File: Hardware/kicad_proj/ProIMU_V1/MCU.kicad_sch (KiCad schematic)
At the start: 8 parts

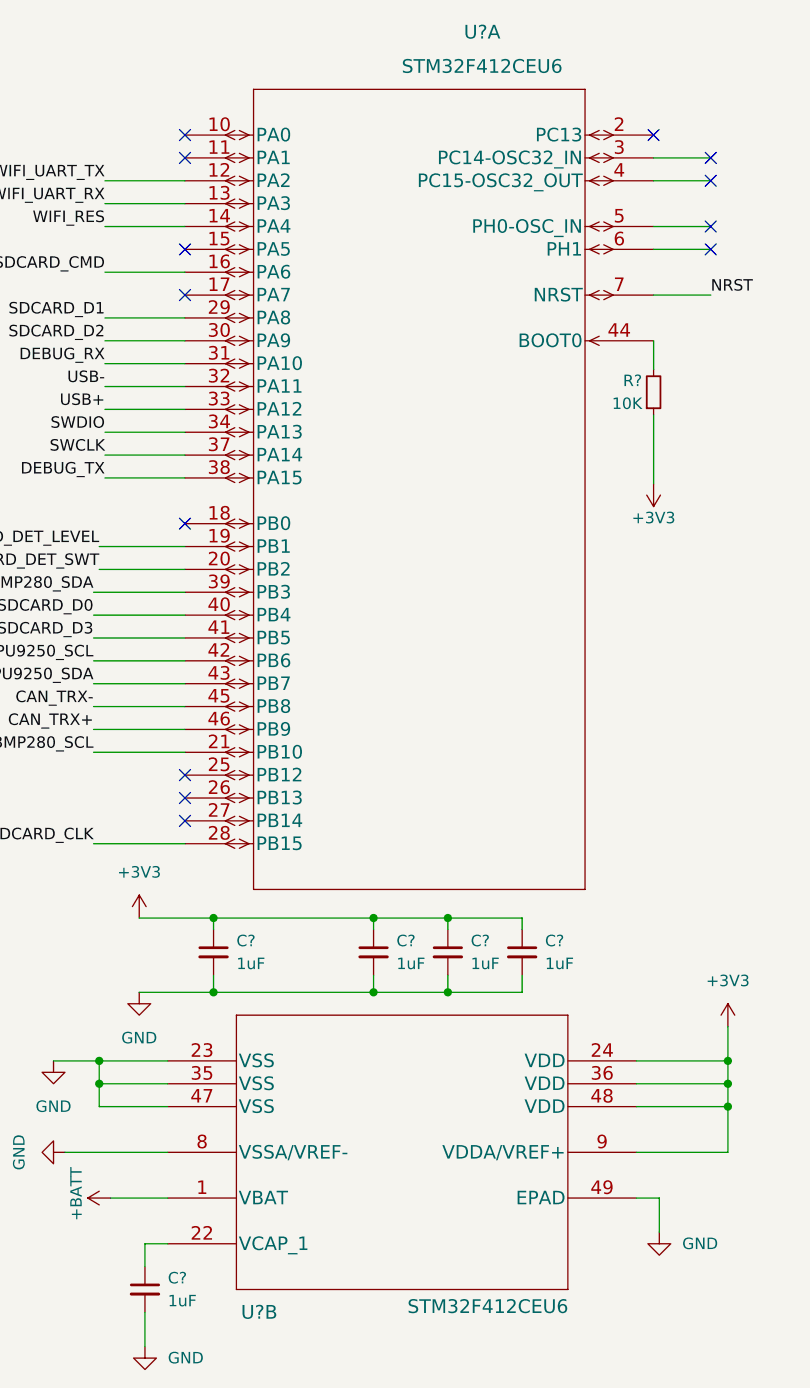
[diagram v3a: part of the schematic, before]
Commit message: Layout Updated. CAN and RS485 section to be updated
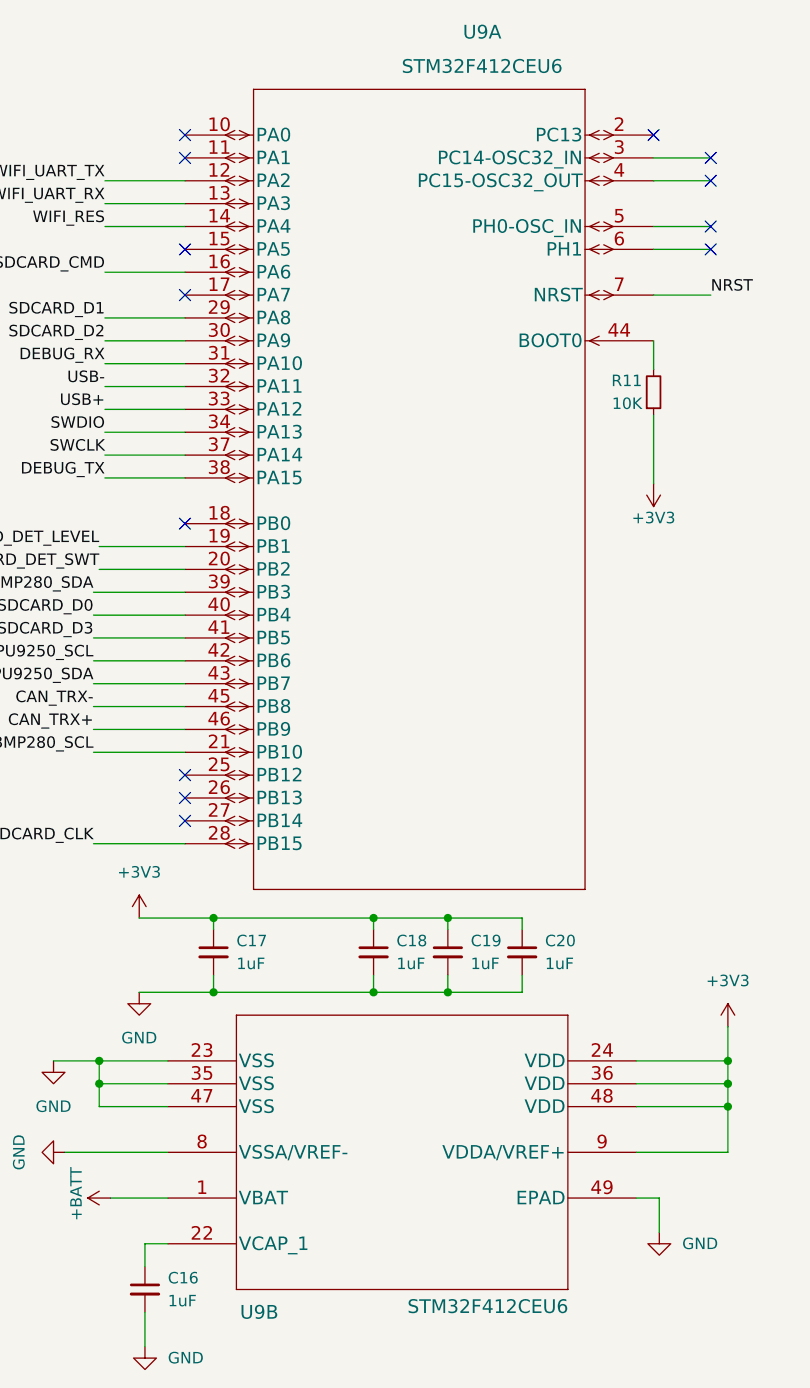
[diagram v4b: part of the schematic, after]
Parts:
- gave numbers to parts that had none: 7
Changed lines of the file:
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@@
   (symbol (lib_id "power:+3V3") (at 163.195 73.025 180) (unit 1)
     (in_bom yes) (on_board yes)
-    (property "Reference" "#PWR?" (id 0) (at 163.195 69.215 0)
+    (property "Reference" "#PWR061" (id 0) (at 163.195 69.215 0)
       (effects (font (size 1.27 1.27)) hide)
     )
@@
   (symbol (lib_id "2022-02-05_19-28-45:STM32F412CEU6") (at 109.22 137.16 0) (unit 2)
     (in_bom yes) (on_board yes)
-    (property "Reference" "U?" (id 0) (at 119.38 165.1 0)
+    (property "Reference" "U9" (id 0) (at 119.38 165.1 0)
       (effects (font (size 1.524 1.524)))
     )
@@
   (symbol (lib_id "Device:C_Small") (at 148.59 125.095 0) (unit 1)
     (in_bom yes) (on_board yes) (fields_autoplaced)
-    (property "Reference" "C?" (id 0) (at 151.13 123.8312 0)
+    (property "Reference" "C20" (id 0) (at 151.13 123.8312 0)
       (effects (font (size 1.27 1.27)) (justify left))
     )
@@
   (symbol (lib_id "power:+3V3") (at 106.045 121.285 0) (unit 1)
     (in_bom yes) (on_board yes) (fields_autoplaced)
-    (property "Reference" "#PWR?" (id 0) (at 106.045 125.095 0)
+    (property "Reference" "#PWR058" (id 0) (at 106.045 125.095 0)
       (effects (font (size 1.27 1.27)) hide)
     )
@@
   (symbol (lib_id "power:+BATT") (at 102.87 152.4 90) (unit 1)
     (in_bom yes) (on_board yes)
-    (property "Reference" "#PWR?" (id 0) (at 106.68 152.4 0)
+    (property "Reference" "#PWR057" (id 0) (at 106.68 152.4 0)
       (effects (font (size 1.27 1.27)) hide)
     )
@@
   (symbol (lib_id "power:GND") (at 163.83 156.21 0) (unit 1)
     (in_bom yes) (on_board yes) (fields_autoplaced)
-    (property "Reference" "#PWR?" (id 0) (at 163.83 162.56 0)
+    (property "Reference" "#PWR062" (id 0) (at 163.83 162.56 0)
       (effects (font (size 1.27 1.27)) hide)
     )
@@
   (symbol (lib_id "power:GND") (at 106.045 129.54 0) (unit 1)
     (in_bom yes) (on_board yes) (fields_autoplaced)
-    (property "Reference" "#PWR?" (id 0) (at 106.045 135.89 0)
+    (property "Reference" "#PWR059" (id 0) (at 106.045 135.89 0)
       (effects (font (size 1.27 1.27)) hide)
     )
@@
   (symbol (lib_id "power:+3V3") (at 171.45 133.35 0) (unit 1)
     (in_bom yes) (on_board yes) (fields_autoplaced)
-    (property "Reference" "#PWR?" (id 0) (at 171.45 137.16 0)
+    (property "Reference" "#PWR063" (id 0) (at 171.45 137.16 0)
       (effects (font (size 1.27 1.27)) hide)
     )
@@
   (symbol (lib_id "Device:R_Small") (at 163.195 62.865 0) (mirror x) (unit 1)
     (in_bom yes) (on_board yes)
-    (property "Reference" "R?" (id 0) (at 161.925 61.595 0)
+    (property "Reference" "R11" (id 0) (at 161.925 61.595 0)
       (effects (font (size 1.27 1.27)) (justify right))
     )
@@
   (symbol (lib_id "power:GND") (at 97.79 147.32 270) (unit 1)
     (in_bom yes) (on_board yes) (fields_autoplaced)
-    (property "Reference" "#PWR?" (id 0) (at 91.44 147.32 0)
+    (property "Reference" "#PWR056" (id 0) (at 91.44 147.32 0)
       (effects (font (size 1.27 1.27)) hide)
     )
@@
   (symbol (lib_id "power:GND") (at 96.52 137.16 0) (unit 1)
     (in_bom yes) (on_board yes) (fields_autoplaced)
-    (property "Reference" "#PWR?" (id 0) (at 96.52 143.51 0)
+    (property "Reference" "#PWR055" (id 0) (at 96.52 143.51 0)
       (effects (font (size 1.27 1.27)) hide)
     )
@@
   (symbol (lib_id "power:GND") (at 106.68 168.91 0) (unit 1)
     (in_bom yes) (on_board yes)
-    (property "Reference" "#PWR?" (id 0) (at 106.68 175.26 0)
+    (property "Reference" "#PWR060" (id 0) (at 106.68 175.26 0)
       (effects (font (size 1.27 1.27)) hide)
     )
@@
   (symbol (lib_id "Device:C_Small") (at 106.68 162.56 0) (unit 1)
     (in_bom yes) (on_board yes) (fields_autoplaced)
-    (property "Reference" "C?" (id 0) (at 109.22 161.2962 0)
+    (property "Reference" "C16" (id 0) (at 109.22 161.2962 0)
       (effects (font (size 1.27 1.27)) (justify left))
     )
@@
   (symbol (lib_id "Device:C_Small") (at 140.335 125.095 0) (unit 1)
     (in_bom yes) (on_board yes) (fields_autoplaced)
-    (property "Reference" "C?" (id 0) (at 142.875 123.8312 0)
+    (property "Reference" "C19" (id 0) (at 142.875 123.8312 0)
       (effects (font (size 1.27 1.27)) (justify left))
     )
@@
   (symbol (lib_id "Device:C_Small") (at 132.08 125.095 0) (unit 1)
     (in_bom yes) (on_board yes) (fields_autoplaced)
-    (property "Reference" "C?" (id 0) (at 134.62 123.8312 0)
+    (property "Reference" "C18" (id 0) (at 134.62 123.8312 0)
       (effects (font (size 1.27 1.27)) (justify left))
     )
@@
   (symbol (lib_id "Device:C_Small") (at 114.3 125.095 0) (unit 1)
     (in_bom yes) (on_board yes) (fields_autoplaced)
-    (property "Reference" "C?" (id 0) (at 116.84 123.8312 0)
+    (property "Reference" "C17" (id 0) (at 116.84 123.8312 0)
       (effects (font (size 1.27 1.27)) (justify left))
     )
@@
   (symbol (lib_name "STM32F412CEU6_1") (lib_id "2022-02-05_19-28-45:STM32F412CEU6") (at 111.125 34.29 0) (unit 1)
     (in_bom yes) (on_board yes) (fields_autoplaced)
-    (property "Reference" "U?" (id 0) (at 144.145 22.86 0)
-      (effects (font (size 1.524 1.524)))
-    )
+    (property "Reference" "U9" (id 0) (at 144.145 22.86 0)
+      (effects (font (size 1.524 1.524)))
+    )

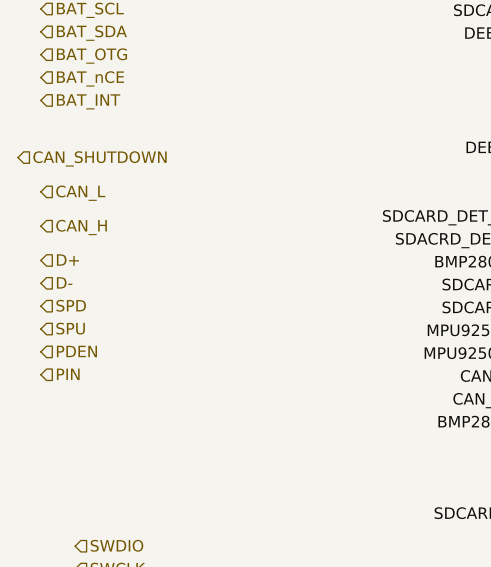
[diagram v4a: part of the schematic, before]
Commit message: Updated Schematic and Layout. Needs more refining
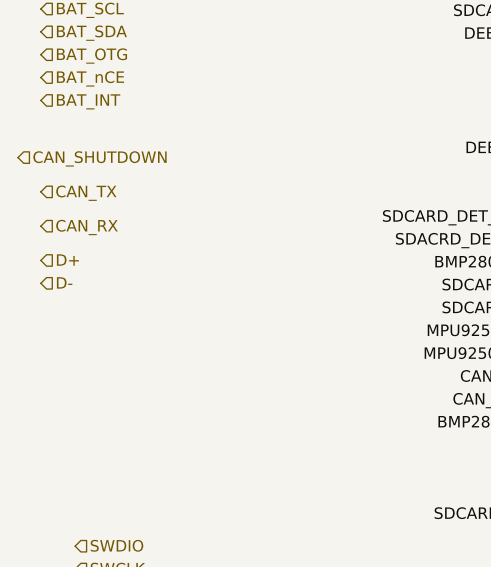
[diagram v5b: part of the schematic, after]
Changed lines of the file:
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@@
     (effects (font (size 1.27 1.27)) (justify left))
   )
-  (hierarchical_label "CAN_L" (shape input) (at 45.72 76.2 0)
+  (hierarchical_label "CAN_TX" (shape input) (at 45.72 76.2 0)
     (effects (font (size 1.27 1.27)) (justify left))
   )
   (hierarchical_label "SDCARD_DET_LEVEL" (shape input) (at 245.11 139.7 0)
-    (effects (font (size 1.27 1.27)) (justify left))
-  )
-  (hierarchical_label "SPU" (shape input) (at 45.72 91.44 0)
     (effects (font (size 1.27 1.27)) (justify left))
   )
@@
     (effects (font (size 1.27 1.27)) (justify left))
   )
-  (hierarchical_label "PIN" (shape input) (at 45.72 96.52 0)
-    (effects (font (size 1.27 1.27)) (justify left))
-  )
   (hierarchical_label "BAT_SDA" (shape input) (at 45.72 58.42 0)
     (effects (font (size 1.27 1.27)) (justify left))
   )
-  (hierarchical_label "CAN_H" (shape input) (at 45.72 80.01 0)
+  (hierarchical_label "CAN_RX" (shape input) (at 45.72 80.01 0)
     (effects (font (size 1.27 1.27)) (justify left))
   )
@@
     (effects (font (size 1.27 1.27)) (justify left))
   )
-  (hierarchical_label "SPD" (shape input) (at 45.72 88.9 0)
-    (effects (font (size 1.27 1.27)) (justify left))
-  )
   (hierarchical_label "SWCLK" (shape input) (at 49.53 118.11 0)
     (effects (font (size 1.27 1.27)) (justify left))
@@
     (effects (font (size 1.27 1.27)) (justify left))
   )
-  (hierarchical_label "PDEN" (shape input) (at 45.72 93.98 0)
-    (effects (font (size 1.27 1.27)) (justify left))
-  )

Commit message: Updated repo
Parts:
- added C1: 1uF, Capacitor_SMD:C_0402_1005Metric_Pad0.74x0.62mm_HandSolder, symbol Device:C_Small
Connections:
- net +3V3: now also C1.1
- net GND: now also C1.2
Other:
- moved on the sheet: C17, C18, C19, C20

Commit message: Updated Schematic
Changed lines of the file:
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@@
     (effects (font (size 1.27 1.27)) (justify left))
+  )
+  (hierarchical_label "SCL" (shape input) (at 58.42 162.56 180)
+    (effects (font (size 1.27 1.27)) (justify right))
   )
   (hierarchical_label "BAT_SCL" (shape input) (at 45.72 55.88 0)
@@
     (effects (font (size 1.27 1.27)) (justify left))
   )
+  (hierarchical_label "nCE" (shape input) (at 227.33 50.8 180)
+    (effects (font (size 1.27 1.27)) (justify right))
+  )
   (hierarchical_label "CAN_TX" (shape input) (at 45.72 76.2 0)
     (effects (font (size 1.27 1.27)) (justify left))
   )
+  (hierarchical_label "nCE" (shape input) (at 58.42 154.94 180)
+    (effects (font (size 1.27 1.27)) (justify right))
+  )
   (hierarchical_label "SDCARD_DET_LEVEL" (shape input) (at 245.11 139.7 0)
     (effects (font (size 1.27 1.27)) (justify left))
+  )
+  (hierarchical_label "SCL" (shape input) (at 227.33 58.42 180)
+    (effects (font (size 1.27 1.27)) (justify right))
   )
   (hierarchical_label "RS232_RX" (shape input) (at 45.72 31.75 0)
@@
   (hierarchical_label "MPU9250_SCK" (shape input) (at 191.77 87.63 0)
     (effects (font (size 1.27 1.27)) (justify left))
+  )
+  (hierarchical_label "OTG" (shape input) (at 58.42 152.4 180)
+    (effects (font (size 1.27 1.27)) (justify right))
+  )
+  (hierarchical_label "SDA" (shape input) (at 227.33 55.88 180)
+    (effects (font (size 1.27 1.27)) (justify right))
   )
   (hierarchical_label "BMP280_SCK" (shape input) (at 191.77 99.06 0)
@@
     (effects (font (size 1.27 1.27)) (justify left))
   )
+  (hierarchical_label "OTG" (shape input) (at 227.33 48.26 180)
+    (effects (font (size 1.27 1.27)) (justify right))
+  )
   (hierarchical_label "BAT_OTG" (shape input) (at 45.72 60.96 0)
     (effects (font (size 1.27 1.27)) (justify left))
@@
   (hierarchical_label "D-" (shape input) (at 45.72 86.36 0)
     (effects (font (size 1.27 1.27)) (justify left))
+  )
+  (hierarchical_label "INT" (shape input) (at 58.42 157.48 180)
+    (effects (font (size 1.27 1.27)) (justify right))
   )
   (hierarchical_label "WIFI_UART_TX" (shape input) (at 48.26 44.45 0)
@@
     (effects (font (size 1.27 1.27)) (justify left))
   )
+  (hierarchical_label "SDA" (shape input) (at 58.42 160.02 180)
+    (effects (font (size 1.27 1.27)) (justify right))
+  )
+  (hierarchical_label "INT" (shape input) (at 227.33 53.34 180)
+    (effects (font (size 1.27 1.27)) (justify right))
+  )
   (hierarchical_label "DEBUG_UART_RX" (shape input) (at 49.53 123.19 0)
